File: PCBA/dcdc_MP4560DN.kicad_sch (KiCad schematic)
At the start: 1 part

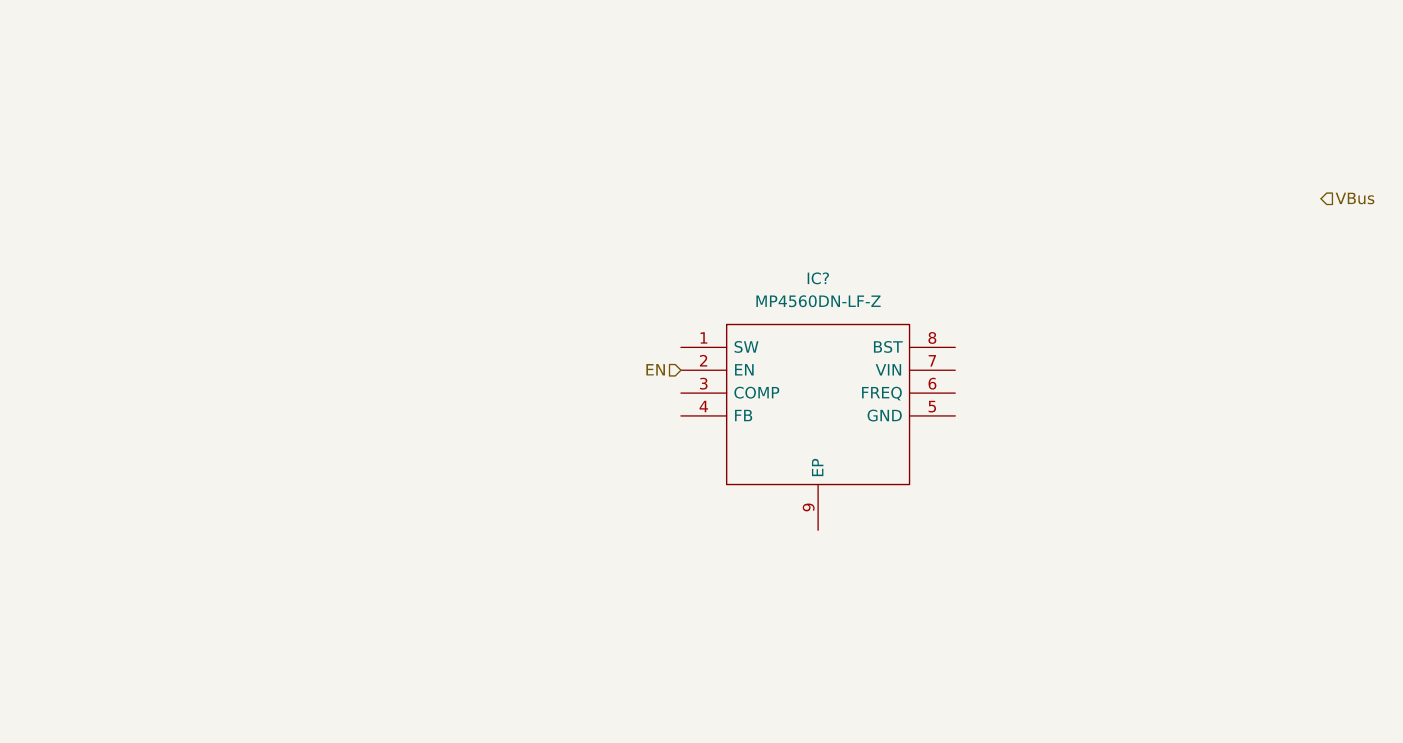
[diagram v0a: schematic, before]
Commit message: Finish MP schematic
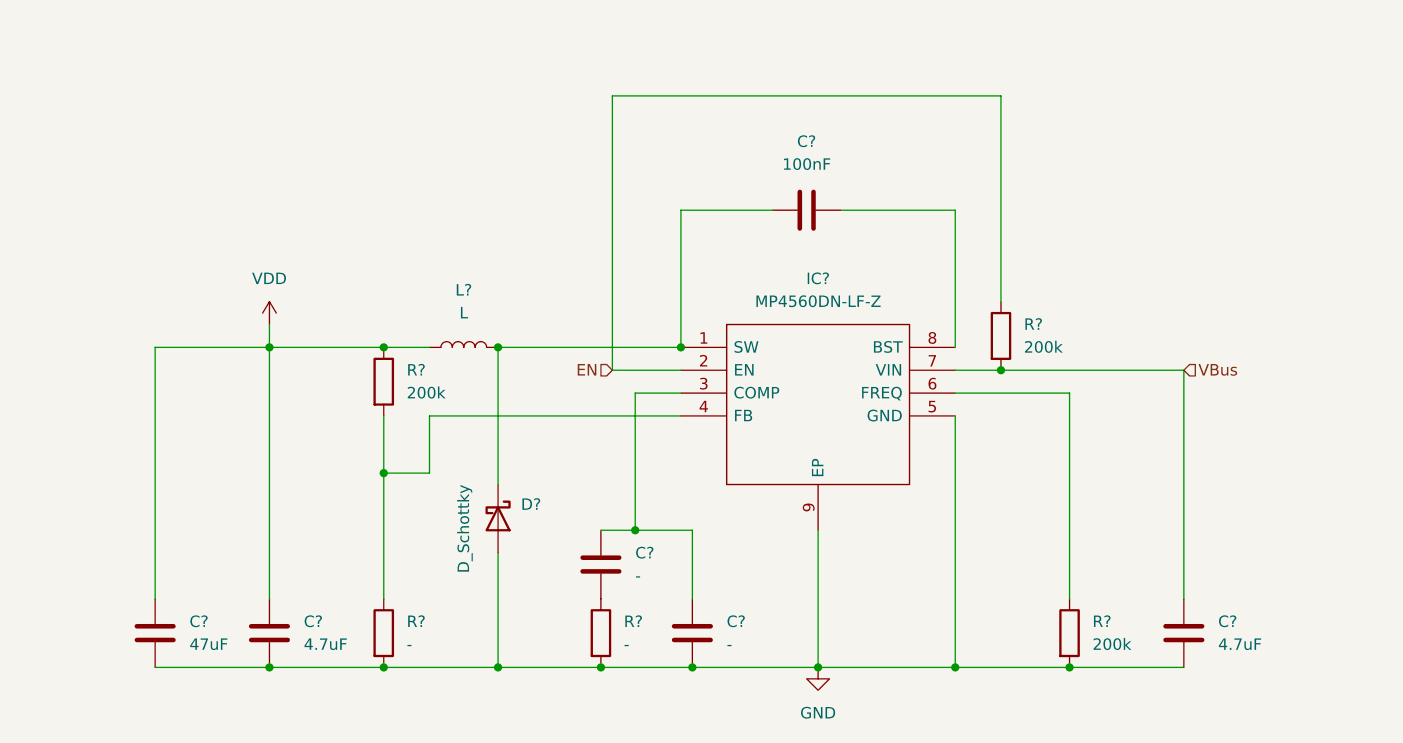
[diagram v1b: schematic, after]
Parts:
- added C? (x2): 4.7uF, symbol Device:C
- added C? (x2): -, symbol Device:C
- added C?: 100nF, symbol Device:C
- added C?: 47uF, symbol Device:C
- added D?: D_Schottky, symbol Device:D_Schottky
- added L?: L, symbol Device:L
- added R? (x3): 200k, symbol Device:R
- added R? (x2): -, symbol Device:R
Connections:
- net EN: now also R?.1
- net VBus: now also IC?.7 (VIN), C?.2, R?.2
- net at IC?.1 (SW): now also C?.1, D?.1 (K), L?.2
- net at IC?.3 (COMP): now also C?.2, C?.2
- net at IC?.4 (FB): now also R?.1, R?.2
- net GND: now reaches IC?.5 (GND)
- net GND: now also IC?.9 (EP), C?.1, C?.1, C?.1, C?.1, D?.2 (A), R?.2, R?.2, R?.2
- net at IC?.6 (FREQ): now also R?.1
- net at IC?.8 (BST): now also C?.2
- new net: C?.1, R?.1
- new net VDD: C?.2, C?.2, L?.1, R?.1

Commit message: Assign footprints
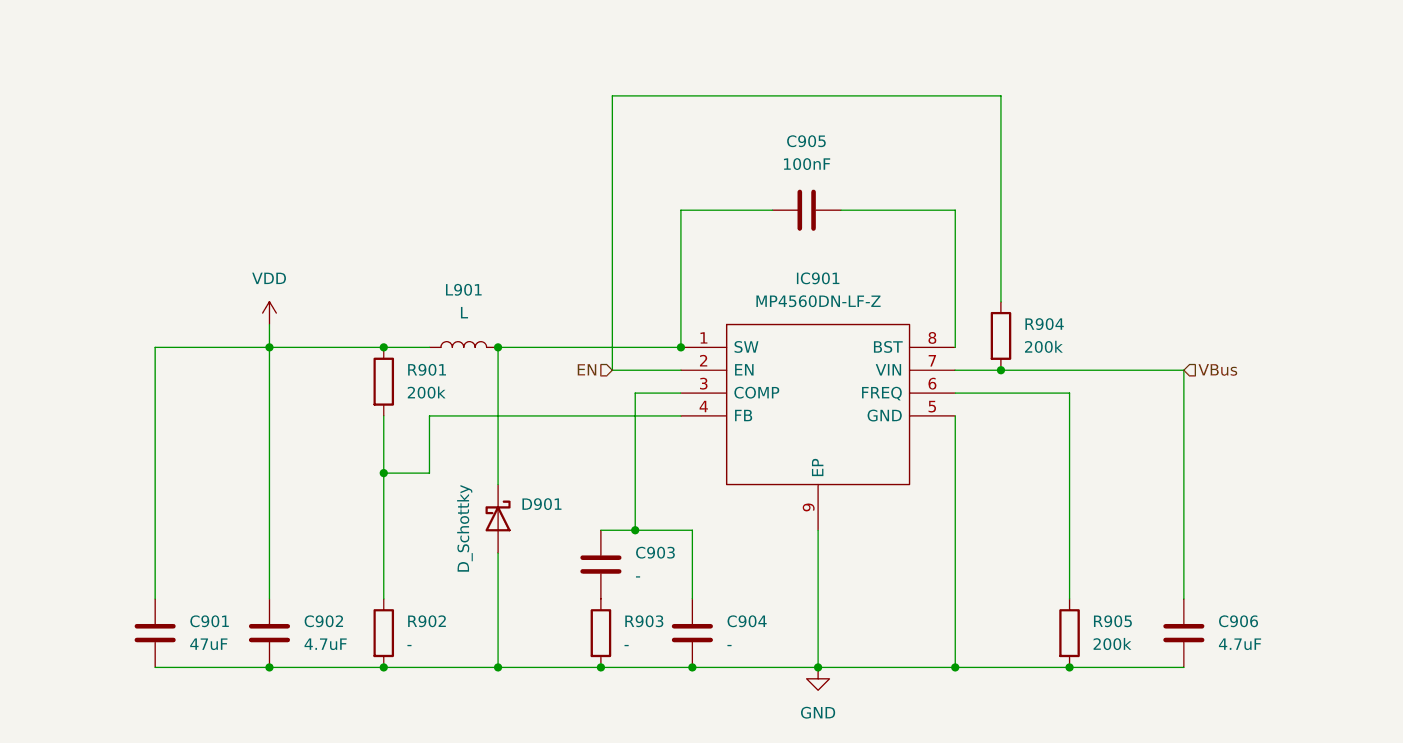
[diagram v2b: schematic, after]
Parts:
- C901, C902, C903, C904, C905, C906: renamed from C?; footprint (none) -> Capacitor_SMD:C_0603_1608Metric
- D901: renamed from D?; footprint (none) -> Diode_SMD:D_SOD-323
- IC901: renamed from IC?; footprint SOIC127P600X170-9N -> MP4560DN:SOIC127P600X170-9N
- R901, R902, R903, R904, R905: renamed from R?; footprint (none) -> Resistor_SMD:R_0603_1608Metric
- gave numbers to parts that had none: 1
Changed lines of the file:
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@@
   (symbol (lib_id "Device:R") (at 144.78 90.17 0) (unit 1)
     (in_bom yes) (on_board yes) (fields_autoplaced)
-    (property "Reference" "R?" (id 0) (at 147.32 88.8999 0)
+    (property "Reference" "R904" (id 0) (at 147.32 88.8999 0)
       (effects (font (size 1.27 1.27)) (justify left))
     )
@@
       (effects (font (size 1.27 1.27)) (justify left))
     )
-    (property "Footprint" "" (id 2) (at 143.002 90.17 90)
+    (property "Footprint" "Resistor_SMD:R_0603_1608Metric" (id 2) (at 143.002 90.17 90)
       (effects (font (size 1.27 1.27)) hide)
     )
@@
   (symbol (lib_id "Device:C") (at 165.1 123.19 180) (unit 1)
     (in_bom yes) (on_board yes) (fields_autoplaced)
-    (property "Reference" "C?" (id 0) (at 168.91 121.9199 0)
+    (property "Reference" "C906" (id 0) (at 168.91 121.9199 0)
       (effects (font (size 1.27 1.27)) (justify right))
     )
@@
       (effects (font (size 1.27 1.27)) (justify right))
     )
-    (property "Footprint" "" (id 2) (at 164.1348 119.38 0)
+    (property "Footprint" "Capacitor_SMD:C_0603_1608Metric" (id 2) (at 164.1348 119.38 0)
       (effects (font (size 1.27 1.27)) hide)
     )
@@
   (symbol (lib_id "Device:D_Schottky") (at 88.9 110.49 270) (unit 1)
     (in_bom yes) (on_board yes)
-    (property "Reference" "D?" (id 0) (at 91.44 108.9024 90)
+    (property "Reference" "D901" (id 0) (at 91.44 108.9024 90)
       (effects (font (size 1.27 1.27)) (justify left))
     )
@@
       (effects (font (size 1.27 1.27)) (justify left))
     )
-    (property "Footprint" "" (id 2) (at 88.9 110.49 0)
+    (property "Footprint" "Diode_SMD:D_SOD-323" (id 2) (at 88.9 110.49 0)
       (effects (font (size 1.27 1.27)) hide)
     )
@@
   (symbol (lib_id "Device:C") (at 63.5 123.19 180) (unit 1)
     (in_bom yes) (on_board yes) (fields_autoplaced)
-    (property "Reference" "C?" (id 0) (at 67.31 121.9199 0)
+    (property "Reference" "C902" (id 0) (at 67.31 121.9199 0)
       (effects (font (size 1.27 1.27)) (justify right))
     )
@@
       (effects (font (size 1.27 1.27)) (justify right))
     )
-    (property "Footprint" "" (id 2) (at 62.5348 119.38 0)
+    (property "Footprint" "Capacitor_SMD:C_0603_1608Metric" (id 2) (at 62.5348 119.38 0)
       (effects (font (size 1.27 1.27)) hide)
     )
@@
   (symbol (lib_id "MP4560DN-LF-Z:MP4560DN-LF-Z") (at 109.22 91.44 0) (unit 1)
     (in_bom yes) (on_board yes) (fields_autoplaced)
-    (property "Reference" "IC?" (id 0) (at 124.46 83.82 0))
+    (property "Reference" "IC901" (id 0) (at 124.46 83.82 0))
     (property "Value" "MP4560DN-LF-Z" (id 1) (at 124.46 86.36 0))
-    (property "Footprint" "SOIC127P600X170-9N" (id 2) (at 135.89 88.9 0)
+    (property "Footprint" "MP4560DN:SOIC127P600X170-9N" (id 2) (at 135.89 88.9 0)
       (effects (font (size 1.27 1.27)) (justify left) hide)
     )
@@
   (symbol (lib_id "Device:C") (at 100.33 115.57 180) (unit 1)
     (in_bom yes) (on_board yes) (fields_autoplaced)
-    (property "Reference" "C?" (id 0) (at 104.14 114.2999 0)
+    (property "Reference" "C903" (id 0) (at 104.14 114.2999 0)
       (effects (font (size 1.27 1.27)) (justify right))
     )
@@
       (effects (font (size 1.27 1.27)) (justify right))
     )
-    (property "Footprint" "" (id 2) (at 99.3648 111.76 0)
+    (property "Footprint" "Capacitor_SMD:C_0603_1608Metric" (id 2) (at 99.3648 111.76 0)
       (effects (font (size 1.27 1.27)) hide)
     )
@@
   (symbol (lib_id "Device:C") (at 123.19 76.2 90) (unit 1)
     (in_bom yes) (on_board yes) (fields_autoplaced)
-    (property "Reference" "C?" (id 0) (at 123.19 68.58 90))
+    (property "Reference" "C905" (id 0) (at 123.19 68.58 90))
     (property "Value" "100nF" (id 1) (at 123.19 71.12 90))
-    (property "Footprint" "" (id 2) (at 127 75.2348 0)
+    (property "Footprint" "Capacitor_SMD:C_0603_1608Metric" (id 2) (at 127 75.2348 0)
       (effects (font (size 1.27 1.27)) hide)
     )
@@
   (symbol (lib_id "Device:C") (at 50.8 123.19 180) (unit 1)
     (in_bom yes) (on_board yes) (fields_autoplaced)
-    (property "Reference" "C?" (id 0) (at 54.61 121.9199 0)
+    (property "Reference" "C901" (id 0) (at 54.61 121.9199 0)
       (effects (font (size 1.27 1.27)) (justify right))
     )
@@
       (effects (font (size 1.27 1.27)) (justify right))
     )
-    (property "Footprint" "" (id 2) (at 49.8348 119.38 0)
+    (property "Footprint" "Capacitor_SMD:C_0603_1608Metric" (id 2) (at 49.8348 119.38 0)
       (effects (font (size 1.27 1.27)) hide)
     )
@@
   (symbol (lib_id "Device:R") (at 76.2 123.19 0) (unit 1)
     (in_bom yes) (on_board yes) (fields_autoplaced)
-    (property "Reference" "R?" (id 0) (at 78.74 121.9199 0)
+    (property "Reference" "R902" (id 0) (at 78.74 121.9199 0)
       (effects (font (size 1.27 1.27)) (justify left))
     )
@@
       (effects (font (size 1.27 1.27)) (justify left))
     )
-    (property "Footprint" "" (id 2) (at 74.422 123.19 90)
+    (property "Footprint" "Resistor_SMD:R_0603_1608Metric" (id 2) (at 74.422 123.19 90)
       (effects (font (size 1.27 1.27)) hide)
     )
@@
   (symbol (lib_id "power:VDD") (at 63.5 88.9 0) (unit 1)
     (in_bom yes) (on_board yes) (fields_autoplaced)
-    (property "Reference" "#PWR?" (id 0) (at 63.5 92.71 0)
+    (property "Reference" "#PWR0156" (id 0) (at 63.5 92.71 0)
       (effects (font (size 1.27 1.27)) hide)
     )
@@
   (symbol (lib_id "Device:R") (at 152.4 123.19 0) (unit 1)
     (in_bom yes) (on_board yes) (fields_autoplaced)
-    (property "Reference" "R?" (id 0) (at 154.94 121.9199 0)
+    (property "Reference" "R905" (id 0) (at 154.94 121.9199 0)
       (effects (font (size 1.27 1.27)) (justify left))
     )
@@
       (effects (font (size 1.27 1.27)) (justify left))
     )
-    (property "Footprint" "" (id 2) (at 150.622 123.19 90)
+    (property "Footprint" "Resistor_SMD:R_0603_1608Metric" (id 2) (at 150.622 123.19 90)
       (effects (font (size 1.27 1.27)) hide)
     )
@@
   (symbol (lib_id "Device:R") (at 76.2 95.25 0) (unit 1)
     (in_bom yes) (on_board yes) (fields_autoplaced)
-    (property "Reference" "R?" (id 0) (at 78.74 93.9799 0)
+    (property "Reference" "R901" (id 0) (at 78.74 93.9799 0)
       (effects (font (size 1.27 1.27)) (justify left))
     )
@@
       (effects (font (size 1.27 1.27)) (justify left))
     )
-    (property "Footprint" "" (id 2) (at 74.422 95.25 90)
+    (property "Footprint" "Resistor_SMD:R_0603_1608Metric" (id 2) (at 74.422 95.25 90)
       (effects (font (size 1.27 1.27)) hide)
     )
@@
   (symbol (lib_id "Device:R") (at 100.33 123.19 0) (unit 1)
     (in_bom yes) (on_board yes) (fields_autoplaced)
-    (property "Reference" "R?" (id 0) (at 102.87 121.9199 0)
+    (property "Reference" "R903" (id 0) (at 102.87 121.9199 0)
       (effects (font (size 1.27 1.27)) (justify left))
     )
@@
       (effects (font (size 1.27 1.27)) (justify left))
     )
-    (property "Footprint" "" (id 2) (at 98.552 123.19 90)
+    (property "Footprint" "Resistor_SMD:R_0603_1608Metric" (id 2) (at 98.552 123.19 90)
       (effects (font (size 1.27 1.27)) hide)
     )
@@
   (symbol (lib_id "Device:L") (at 85.09 91.44 90) (unit 1)
     (in_bom yes) (on_board yes) (fields_autoplaced)
-    (property "Reference" "L?" (id 0) (at 85.09 85.09 90))
+    (property "Reference" "L901" (id 0) (at 85.09 85.09 90))
     (property "Value" "L" (id 1) (at 85.09 87.63 90))
     (property "Footprint" "" (id 2) (at 85.09 91.44 0)
@@
   (symbol (lib_id "Device:C") (at 110.49 123.19 180) (unit 1)
     (in_bom yes) (on_board yes) (fields_autoplaced)
-    (property "Reference" "C?" (id 0) (at 114.3 121.9199 0)
+    (property "Reference" "C904" (id 0) (at 114.3 121.9199 0)
       (effects (font (size 1.27 1.27)) (justify right))
     )
@@
       (effects (font (size 1.27 1.27)) (justify right))
     )
-    (property "Footprint" "" (id 2) (at 109.5248 119.38 0)
+    (property "Footprint" "Capacitor_SMD:C_0603_1608Metric" (id 2) (at 109.5248 119.38 0)
       (effects (font (size 1.27 1.27)) hide)
     )
@@
   (symbol (lib_id "power:GND") (at 124.46 127 0) (unit 1)
     (in_bom yes) (on_board yes) (fields_autoplaced)
-    (property "Reference" "#PWR?" (id 0) (at 124.46 133.35 0)
-      (effects (font (size 1.27 1.27)) hide)
-    )
+    (property "Reference" "#PWR0155" (id 0) (at 124.46 133.35 0)
+      (effects (font (size 1.27 1.27)) hide)
+    )

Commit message: Rough outline
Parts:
- L901: value L -> 15; footprint (none) -> Inductor_SMD:L_Wuerth_MAPI-3010
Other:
- note added: "https://lcsc.com/product-detail/Power-Inductors_CENKER-CKCS3012-15uH-M_C354559.html"
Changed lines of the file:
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@@
     (stroke (width 0) (type default) (color 0 0 0 0))
+  )
+  (text "https://lcsc.com/product-detail/Power-Inductors_CENKER-CKCS3012-15uH-M_C354559.html"
+    (at 35.56 57.15 0)
+    (effects (font (size 1.27 1.27)) (justify left bottom))
   )
   (hierarchical_label "EN" (shape input) (at 101.6 93.98 180)
@@
     (in_bom yes) (on_board yes) (fields_autoplaced)
     (property "Reference" "L901" (id 0) (at 85.09 85.09 90))
-    (property "Value" "L" (id 1) (at 85.09 87.63 90))
-    (property "Footprint" "" (id 2) (at 85.09 91.44 0)
-      (effects (font (size 1.27 1.27)) hide)
-    )
+    (property "Value" "15" (id 1) (at 85.09 87.63 90))
+    (property "Footprint" "Inductor_SMD:L_Wuerth_MAPI-3010" (id 2) (at 85.09 91.44 0)
+      (effects (font (size 1.27 1.27)) hide)
+    )

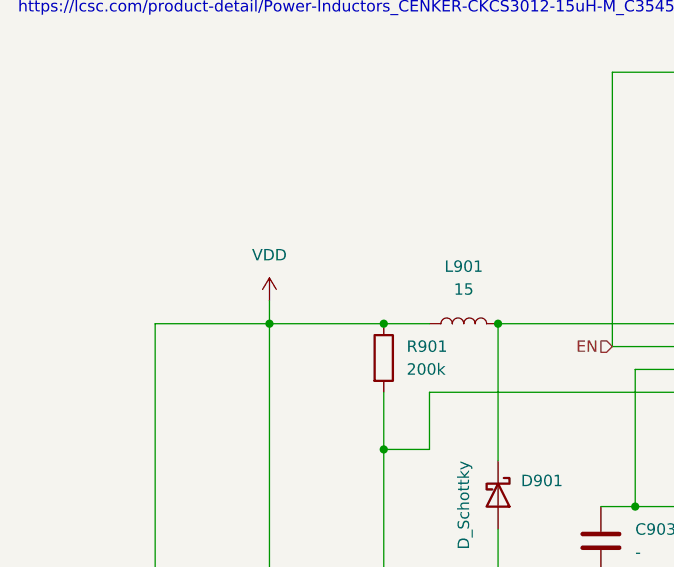
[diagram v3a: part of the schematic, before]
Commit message: Step models for ports
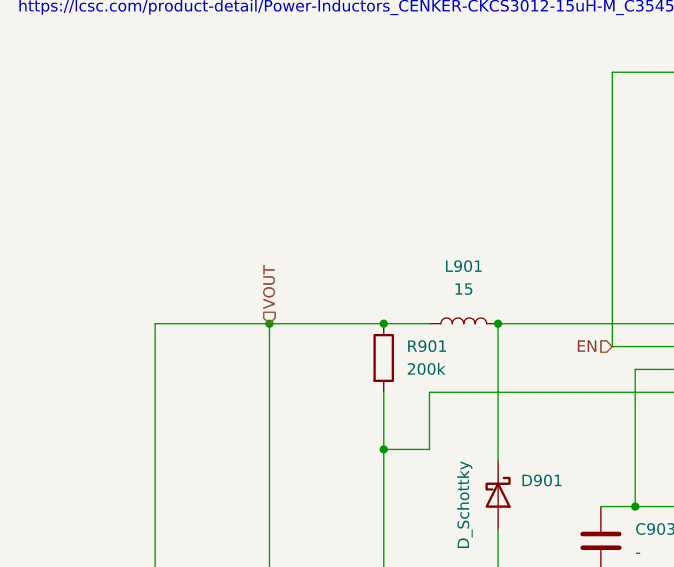
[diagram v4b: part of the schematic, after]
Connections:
- net VDD renamed VOUT
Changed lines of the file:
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@@
-    (stroke (width 0) (type default) (color 0 0 0 0))
-  )
-  (wire (pts (xy 63.5 88.9) (xy 63.5 91.44))
     (stroke (width 0) (type default) (color 0 0 0 0))
   )
@@
   (hierarchical_label "EN" (shape input) (at 101.6 93.98 180)
     (effects (font (size 1.27 1.27)) (justify right))
+  )
+  (hierarchical_label "VOUT" (shape input) (at 63.5 91.44 90)
+    (effects (font (size 1.27 1.27)) (justify left))
   )
   (hierarchical_label "VBus" (shape input) (at 165.1 93.98 0)
@@
     (pin "2")
   )
-  (symbol (lib_id "power:VDD") (at 63.5 88.9 0) (unit 1)
-    (in_bom yes) (on_board yes) (fields_autoplaced)
-    (property "Reference" "#PWR0156" (id 0) (at 63.5 92.71 0)
-      (effects (font (size 1.27 1.27)) hide)
-    )
-    (property "Value" "VDD" (id 1) (at 63.5 83.82 0))
-    (property "Footprint" "" (id 2) (at 63.5 88.9 0)
-      (effects (font (size 1.27 1.27)) hide)
-    )
-    (property "Datasheet" "" (id 3) (at 63.5 88.9 0)
-      (effects (font (size 1.27 1.27)) hide)
-    )
-    (pin "1")
-  )
   (symbol (lib_id "Device:R") (at 152.4 123.19 0) (unit 1)
